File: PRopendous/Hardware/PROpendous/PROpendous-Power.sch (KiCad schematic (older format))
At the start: 46 parts, among them IC2 G07, IC4 811, SW1 RESET, U11 1117-1.2V, U12 1117-Adj

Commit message: Updated files.  DDR SDRAM schematic completed.
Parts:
- removed C17: 4u7, symbol CP_TANTALUM_MINI
- removed C19, C26, C32, C78: 10u, symbol CP_TANTALUM_MINI
- removed C21, C33, C34, C50, C92: 0u1, symbol C_MINI
- removed C28, C35, C62, C70: 10n, symbol C_MINI
- removed C29, C66, C68, C85: 1uF, symbol C_MINI
- removed C38: 220p, symbol C_MINI
- removed C39: 3n9, symbol C_MINI
- removed C40: 3n3, symbol C_MINI
- removed C48: 1u, symbol C_MINI
- removed C79, C86, C88, C90, C91: 4u7, symbol C_MINI
- removed C87: 10u, symbol C_MINI
- removed C89: 22u, symbol C_MINI
- removed D1: BAT54C, symbol BAT54
- removed IC2: G07, symbol 74LVC2G07
- removed IC4: 811, symbol ADM811
- removed L3, L6, L7, L9: FB, symbol L_MINI
- removed R13, R2: 10k, symbol R_MINI
- removed R17: 10, symbol R_MINI
- removed R8: 100k, symbol R_MINI
- removed R86, R91: 120, symbol R_MINI
- removed R92: 168, symbol R_MINI
- removed SW1: RESET, symbol SWITCH_PUSHBUTTON
- removed U11: 1117-1.2V, symbol 1117
- removed U12: 1117-Adj, symbol 1117
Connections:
- net labels added: GND1, GNDPWR, HP_VGND, VDD4V2, VDD5V, VDDA, VDDD, VDDIO_3V3, VDDM_2V5, VDD_BATT, VDD_XTAL
- net labels removed: JTAGSEL, RESET_SUP3, TRST_N, VBUS, VDD12, VDD18, VDD3, VDDA12, VDDA3, VDDA3_USB, VDDI, VSUP1, VSUP3, VSUP4, VSUP8, VSYS, ^JTAG_SRST, nRST
- wire segments 71 -> 12
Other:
- note added: "Notes:\n - All capacitors are X5R, 6.3V, 20% or better unless otherwise noted\n - VDDIO, VDDD, VDDA should have 33uF of decoupling and LPF >1MHz per IMX23RM Pg#1277"
- note removed: "1%"
- note removed: "1.2V"
- note removed: "2.93V"
- note removed: "3V"
- note removed: "74LVC2G07"
- note removed: "JTAGSEL and ^JTAG_TRST have pull-up resistors near JTAG connector"
- note removed: "R92 = 120((Vout/1.25)-1)"
- note removed: "RESET Circuitry"
- note removed: "USB_VDDA_DRV"
- note removed: "VDDE_IOA"
- note removed: "VDDE_IOB"
- note removed: "VDDE_IOC"
- note removed: "up to 800mA"

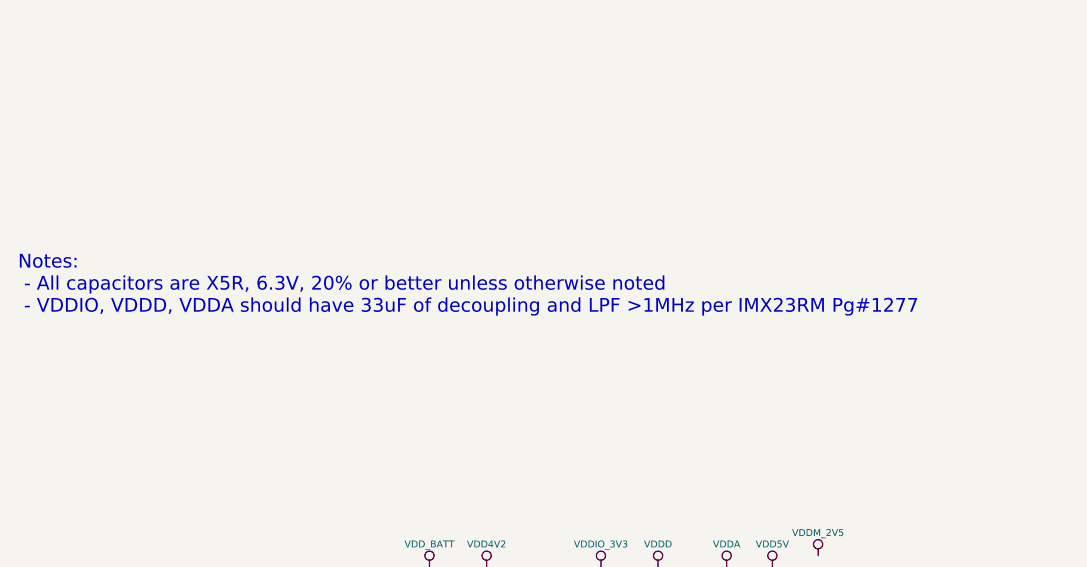
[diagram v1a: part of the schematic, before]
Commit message: Updated PROpendous i.MX233 project.  DDR SDRAM layout is complete.
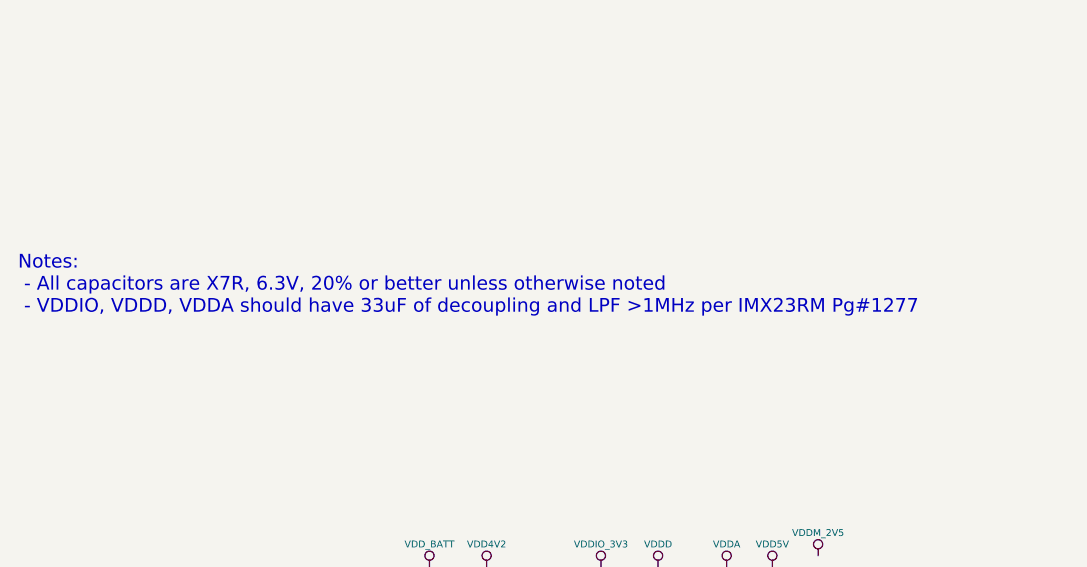
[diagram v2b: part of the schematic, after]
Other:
- note added: "Notes:\n - All capacitors are X7R, 6.3V, 20% or better unless otherwise noted\n - VDDIO, VDDD, VDDA should have 33uF of decoupling and LPF >1MHz per IMX23RM Pg#1277"
- note removed: "Notes:\n - All capacitors are X5R, 6.3V, 20% or better unless otherwise noted\n - VDDIO, VDDD, VDDA should have 33uF of decoupling and LPF >1MHz per IMX23RM Pg#1277"
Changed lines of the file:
@@
-EESchema Schematic File Version 2  date 07/04/2010 20:14:10
+EESchema Schematic File Version 2  date 17/04/2010 17:25:37
 LIBS:opendous
 LIBS:device
@@
 EELAYER END
 $Descr A4 11700 8267
-Sheet 4 6
+Sheet 6 7
 Title "PROpendous"
-Date "8 apr 2010"
+Date "17 apr 2010"
 Rev "1.0"
 Comp "Opendous Inc. (www.opendous.org)"
@@
 $EndDescr
 $Comp
-L GNDPWR #PWR026
+L GNDPWR #PWR042
 U 1 1 4BBD1AE8
 P 6800 7550
-F 0 "#PWR026" H 6800 7600 40  0001 C CNN
+F 0 "#PWR042" H 6800 7600 40  0001 C CNN
 F 1 "GNDPWR" H 6800 7490 25  0000 C CNN
 	1    6800 7550
@@
 	6800 7550 6800 7500
 $Comp
-L PWR_FLAG #FLG027
+L PWR_FLAG #FLG043
 U 1 1 4BBD1AE5
 P 6800 7500
-F 0 "#FLG027" H 6800 7770 30  0001 C CNN
+F 0 "#FLG043" H 6800 7770 30  0001 C CNN
 F 1 "PWR_FLAG" H 6800 7730 30  0000 C CNN
 	1    6800 7500
@@
 $EndComp
 $Comp
-L HP_VGND #PWR028
+L HP_VGND #PWR044
 U 1 1 4BBCE7C1
 P 6550 7550
-F 0 "#PWR028" H 6550 7550 30  0001 C CNN
+F 0 "#PWR044" H 6550 7550 30  0001 C CNN
 F 1 "HP_VGND" H 6550 7480 30  0000 C CNN
 	1    6550 7550
@@
 $EndComp
 $Comp
-L PWR_FLAG #FLG029
+L PWR_FLAG #FLG045
 U 1 1 4BBCE66D
 P 6550 7500
-F 0 "#FLG029" H 6550 7770 30  0001 C CNN
+F 0 "#FLG045" H 6550 7770 30  0001 C CNN
 F 1 "PWR_FLAG" H 6550 7730 30  0000 C CNN
 	1    6550 7500
@@
 	5550 7400 5550 7350
 $Comp
-L GND #PWR030
+L GND #PWR046
 U 1 1 4BBCDADD
 P 6050 7550
-F 0 "#PWR030" H 6050 7550 30  0001 C CNN
+F 0 "#PWR046" H 6050 7550 30  0001 C CNN
 F 1 "GND" H 6050 7480 30  0001 C CNN
 	1    6050 7550
@@
 $EndComp
 $Comp
-L GND1 #PWR031
+L GND1 #PWR047
 U 1 1 4BBCDAD7
 P 6300 7550
-F 0 "#PWR031" H 6300 7550 30  0001 C CNN
+F 0 "#PWR047" H 6300 7550 30  0001 C CNN
 F 1 "GND1" H 6300 7480 30  0000 C CNN
 	1    6300 7550
@@
 $EndComp
 $Comp
-L PWR_FLAG #FLG032
+L PWR_FLAG #FLG048
 U 1 1 4BBCDAD6
 P 6300 7500
-F 0 "#FLG032" H 6300 7770 30  0001 C CNN
+F 0 "#FLG048" H 6300 7770 30  0001 C CNN
 F 1 "PWR_FLAG" H 6300 7730 30  0000 C CNN
 	1    6300 7500
@@
 $EndComp
 $Comp
-L PWR_FLAG #FLG033
+L PWR_FLAG #FLG049
 U 1 1 4BBCDABF
 P 6050 7500
-F 0 "#FLG033" H 6050 7770 30  0001 C CNN
+F 0 "#FLG049" H 6050 7770 30  0001 C CNN
 F 1 "PWR_FLAG" H 6050 7730 30  0000 C CNN
 	1    6050 7500
@@
 $EndComp
 $Comp
-L PWR_FLAG #FLG034
+L PWR_FLAG #FLG050
 U 1 1 4BBCDA9A
 P 5300 7400
-F 0 "#FLG034" H 5300 7670 30  0001 C CNN
+F 0 "#FLG050" H 5300 7670 30  0001 C CNN
 F 1 "PWR_FLAG" H 5300 7630 30  0000 C CNN
 	1    5300 7400
@@
 $EndComp
 $Comp
-L PWR_FLAG #FLG035
+L PWR_FLAG #FLG051
 U 1 1 4BBCDA99
 P 5050 7400
-F 0 "#FLG035" H 5050 7670 30  0001 C CNN
+F 0 "#FLG051" H 5050 7670 30  0001 C CNN
 F 1 "PWR_FLAG" H 5050 7630 30  0000 C CNN
 	1    5050 7400
@@
 $EndComp
 $Comp
-L PWR_FLAG #FLG036
+L PWR_FLAG #FLG052
 U 1 1 4BBCDA98
 P 5550 7400
-F 0 "#FLG036" H 5550 7670 30  0001 C CNN
+F 0 "#FLG052" H 5550 7670 30  0001 C CNN
 F 1 "PWR_FLAG" H 5550 7630 30  0000 C CNN
 	1    5550 7400
@@
 $EndComp
 $Comp
-L PWR_FLAG #FLG037
+L PWR_FLAG #FLG053
 U 1 1 4BBCDA97
 P 5800 7400
-F 0 "#FLG037" H 5800 7670 30  0001 C CNN
+F 0 "#FLG053" H 5800 7670 30  0001 C CNN
 F 1 "PWR_FLAG" H 5800 7630 30  0000 C CNN
 	1    5800 7400
@@
 $EndComp
 $Comp
-L PWR_FLAG #FLG038
+L PWR_FLAG #FLG054
 U 1 1 4BBCDA95
 P 4800 7400
-F 0 "#FLG038" H 4800 7670 30  0001 C CNN
+F 0 "#FLG054" H 4800 7670 30  0001 C CNN
 F 1 "PWR_FLAG" H 4800 7630 30  0000 C CNN
 	1    4800 7400
@@
 $EndComp
 $Comp
-L PWR_FLAG #FLG039
+L PWR_FLAG #FLG055
 U 1 1 4BBCDA94
 P 4550 7400
-F 0 "#FLG039" H 4550 7670 30  0001 C CNN
+F 0 "#FLG055" H 4550 7670 30  0001 C CNN
 F 1 "PWR_FLAG" H 4550 7630 30  0000 C CNN
 	1    4550 7400
@@
 $EndComp
 $Comp
-L PWR_FLAG #FLG040
+L PWR_FLAG #FLG056
 U 1 1 4BBCDA8D
 P 4050 7400
-F 0 "#FLG040" H 4050 7670 30  0001 C CNN
+F 0 "#FLG056" H 4050 7670 30  0001 C CNN
 F 1 "PWR_FLAG" H 4050 7630 30  0000 C CNN
 	1    4050 7400
@@
 $EndComp
 $Comp
-L PWR_FLAG #FLG041
+L PWR_FLAG #FLG057
 U 1 1 4BBCDA84
 P 4300 7400
-F 0 "#FLG041" H 4300 7670 30  0001 C CNN
+F 0 "#FLG057" H 4300 7670 30  0001 C CNN
 F 1 "PWR_FLAG" H 4300 7630 30  0000 C CNN
 	1    4300 7400
@@
 $EndComp
 $Comp
-L VDDM_2V5 #PWR042
+L VDDM_2V5 #PWR058
 U 1 1 4BBCDA81
 P 5800 7350
-F 0 "#PWR042" H 5800 7450 30  0001 C CNN
+F 0 "#PWR058" H 5800 7450 30  0001 C CNN
 F 1 "VDDM_2V5" H 5800 7450 30  0000 C CNN
 	1    5800 7350
@@
 $EndComp
 $Comp
-L VDD_XTAL #PWR043
+L VDD_XTAL #PWR059
 U 1 1 4BBCDA80
 P 4050 7350
-F 0 "#PWR043" H 4050 7450 30  0001 C CNN
+F 0 "#PWR059" H 4050 7450 30  0001 C CNN
 F 1 "VDD_XTAL" H 4050 7450 30  0000 C CNN
 	1    4050 7350
@@
 $EndComp
 $Comp
-L VDDA #PWR044
+L VDDA #PWR060
 U 1 1 4BBCDA7F
 P 5300 7350
-F 0 "#PWR044" H 5300 7450 30  0001 C CNN
+F 0 "#PWR060" H 5300 7450 30  0001 C CNN
 F 1 "VDDA" H 5300 7450 30  0000 C CNN
 	1    5300 7350
@@
 $EndComp
 $Comp
-L VDDD #PWR045
+L VDDD #PWR061
 U 1 1 4BBCDA7E
 P 5050 7350
-F 0 "#PWR045" H 5050 7450 30  0001 C CNN
+F 0 "#PWR061" H 5050 7450 30  0001 C CNN
 F 1 "VDDD" H 5050 7450 30  0000 C CNN
 	1    5050 7350
@@
 $EndComp
 $Comp
-L VDDIO_3V3 #PWR046
+L VDDIO_3V3 #PWR062
 U 1 1 4BBCDA7D
 P 4800 7350
-F 0 "#PWR046" H 4800 7450 30  0001 C CNN
+F 0 "#PWR062" H 4800 7450 30  0001 C CNN
 F 1 "VDDIO_3V3" H 4800 7450 30  0000 C CNN
 	1    4800 7350
@@
 $EndComp
 $Comp
-L VDD4V2 #PWR047
+L VDD4V2 #PWR063
 U 1 1 4BBCDA7C
 P 4550 7350
-F 0 "#PWR047" H 4550 7450 30  0001 C CNN
+F 0 "#PWR063" H 4550 7450 30  0001 C CNN
 F 1 "VDD4V2" H 4550 7450 30  0000 C CNN
 	1    4550 7350
@@
 $EndComp
 $Comp
-L VDD_BATT #PWR048
+L VDD_BATT #PWR064
 U 1 1 4BBCDA7B
 P 4300 7350
-F 0 "#PWR048" H 4300 7450 30  0001 C CNN
+F 0 "#PWR064" H 4300 7450 30  0001 C CNN
 F 1 "VDD_BATT" H 4300 7450 30  0000 C CNN
 	1    4300 7350
@@
 $EndComp
 $Comp
-L VDD5V #PWR049
+L VDD5V #PWR065
 U 1 1 4BBCDA7A
 P 5550 7350
-F 0 "#PWR049" H 5550 7450 30  0001 C CNN
+F 0 "#PWR065" H 5550 7450 30  0001 C CNN
 F 1 "VDD5V" H 5550 7450 30  0000 C CNN
 	1    5550 7350
@@
 $EndComp
 $Comp
-L VDD5V #PWR050
+L VDD5V #PWR066
 U 1 1 4BBCD833
 P 3950 1850
-F 0 "#PWR050" H 3950 1950 30  0001 C CNN
+F 0 "#PWR066" H 3950 1950 30  0001 C CNN
 F 1 "VDD5V" H 3950 1950 30  0000 C CNN
 	1    3950 1850
@@
 $EndComp
 Text Notes 650  750  0    60   ~ 0
-Notes:\n - All capacitors are X5R, 6.3V, 20% or better unless otherwise noted\n - VDDIO, VDDD, VDDA should have 33uF of decoupling and LPF >1MHz per IMX23RM Pg#1277
+Notes:\n - All capacitors are X7R, 6.3V, 20% or better unless otherwise noted\n - VDDIO, VDDD, VDDA should have 33uF of decoupling and LPF >1MHz per IMX23RM Pg#1277
 Text Label 9300 -4600 2    40   ~ 0
 LCD_D00
@@
 PSWITCH
 $Comp
-L VDD_BATT #PWR051
+L VDD_BATT #PWR067
 U 1 1 4BBCE209
 P 2450 1850
-F 0 "#PWR051" H 2450 1950 30  0001 C CNN
+F 0 "#PWR067" H 2450 1950 30  0001 C CNN
 F 1 "VDD_BATT" H 2450 1950 30  0000 C CNN
 	1    2450 1850
@@
 $EndComp
 $Comp
-L VDD4V2 #PWR052
+L VDD4V2 #PWR068
 U 1 1 4BBCE208
 P 2700 1850
-F 0 "#PWR052" H 2700 1950 30  0001 C CNN
+F 0 "#PWR068" H 2700 1950 30  0001 C CNN
 F 1 "VDD4V2" H 2700 1950 30  0000 C CNN
 	1    2700 1850
@@
 $EndComp
 $Comp
-L VDDIO_3V3 #PWR053
+L VDDIO_3V3 #PWR069
 U 1 1 4BBCE207
 P 3200 1850
-F 0 "#PWR053" H 3200 1950 30  0001 C CNN
+F 0 "#PWR069" H 3200 1950 30  0001 C CNN
 F 1 "VDDIO_3V3" H 3200 1950 30  0000 C CNN
 	1    3200 1850
@@
 $EndComp
 $Comp
-L VDDD #PWR054
+L VDDD #PWR070
 U 1 1 4BBCCFCD
 P 3450 1850
-F 0 "#PWR054" H 3450 1950 30  0001 C CNN
+F 0 "#PWR070" H 3450 1950 30  0001 C CNN
 F 1 "VDDD" H 3450 1950 30  0000 C CNN
 	1    3450 1850
@@
 $EndComp
 $Comp
-L VDDA #PWR055
+L VDDA #PWR071
 U 1 1 4BBCCFCC
 P 3750 1850
-F 0 "#PWR055" H 3750 1950 30  0001 C CNN
+F 0 "#PWR071" H 3750 1950 30  0001 C CNN
 F 1 "VDDA" H 3750 1950 30  0000 C CNN
 	1    3750 1850
@@
 $EndComp
 $Comp
-L VDDM_2V5 #PWR056
+L VDDM_2V5 #PWR072
 U 1 1 4BBCE203
 P 4150 1800
-F 0 "#PWR056" H 4150 1900 30  0001 C CNN
+F 0 "#PWR072" H 4150 1900 30  0001 C CNN
 F 1 "VDDM_2V5" H 4150 1900 30  0000 C CNN
 	1    4150 1800
